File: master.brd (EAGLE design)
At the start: 56.1 x 93.9 mm, 77 parts, among them M1 DHT22-NP, M2 NRF24L01P-M, Q1 IRLML2502, U1 XMEGA-A3TQFP, U2 DS1302SOIC, U3 25LC640A-E/SN, U4 ENC28J60SO, U5 TS1117, X1 serial, X2 SPI/1W, X3 I2C, X4 ADC, X6 PS25_3W-R, X7 PS25_3W-R, X8 PS25_3W-R, X9 PS25_3W-R, Y1 25MHz

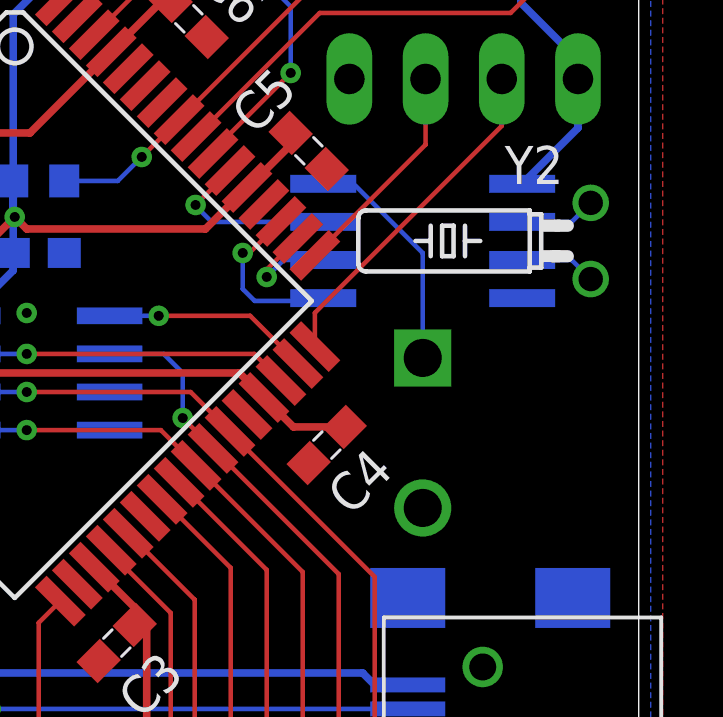
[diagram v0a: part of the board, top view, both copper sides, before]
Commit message: decoupling cap for rtc
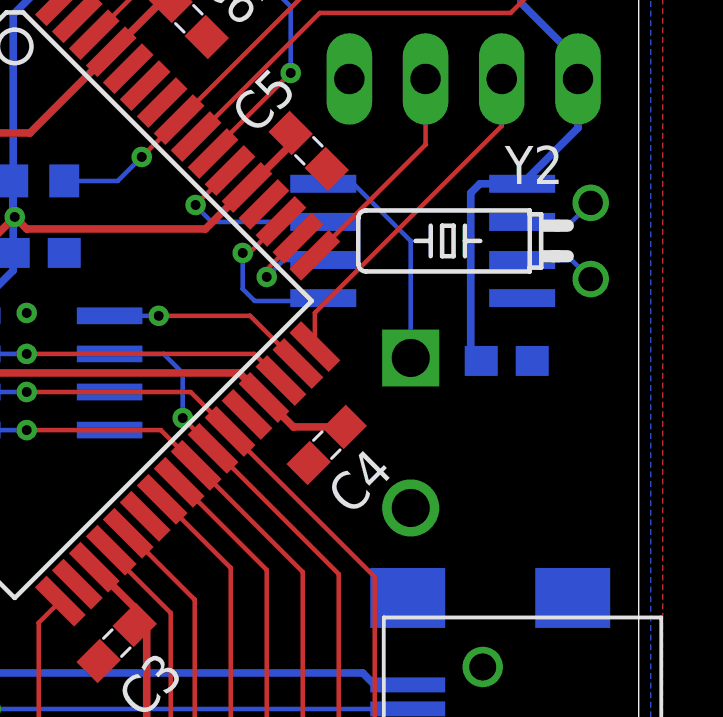
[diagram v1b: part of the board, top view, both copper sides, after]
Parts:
- added C24: 100n, rcl:C0603
- moved C14 0.40 mm to (48.4, 64.4)
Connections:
- net GND: now also C24.2
- net VCC: now also C24.1
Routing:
- net VCC: track 385.5 -> 393.1 mm

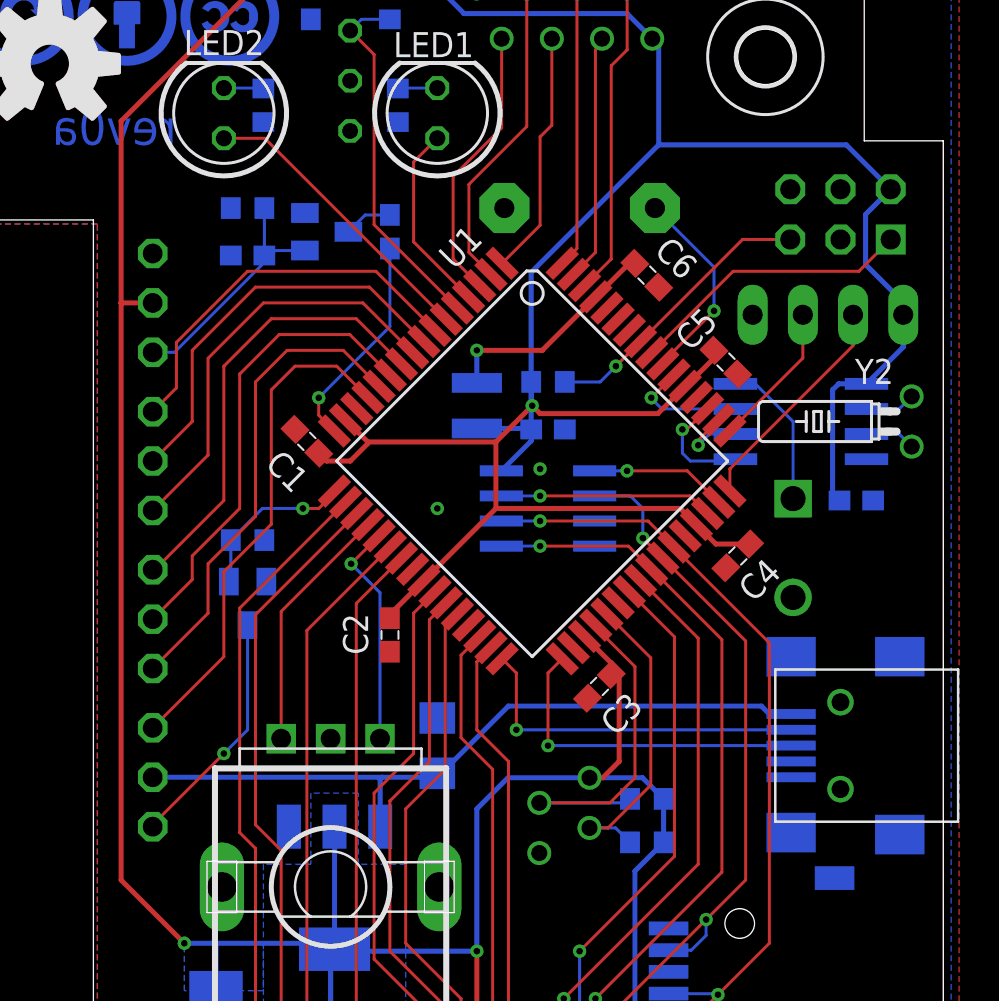
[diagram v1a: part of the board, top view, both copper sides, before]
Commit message: lcd connector changed to standard 2.54 pin header
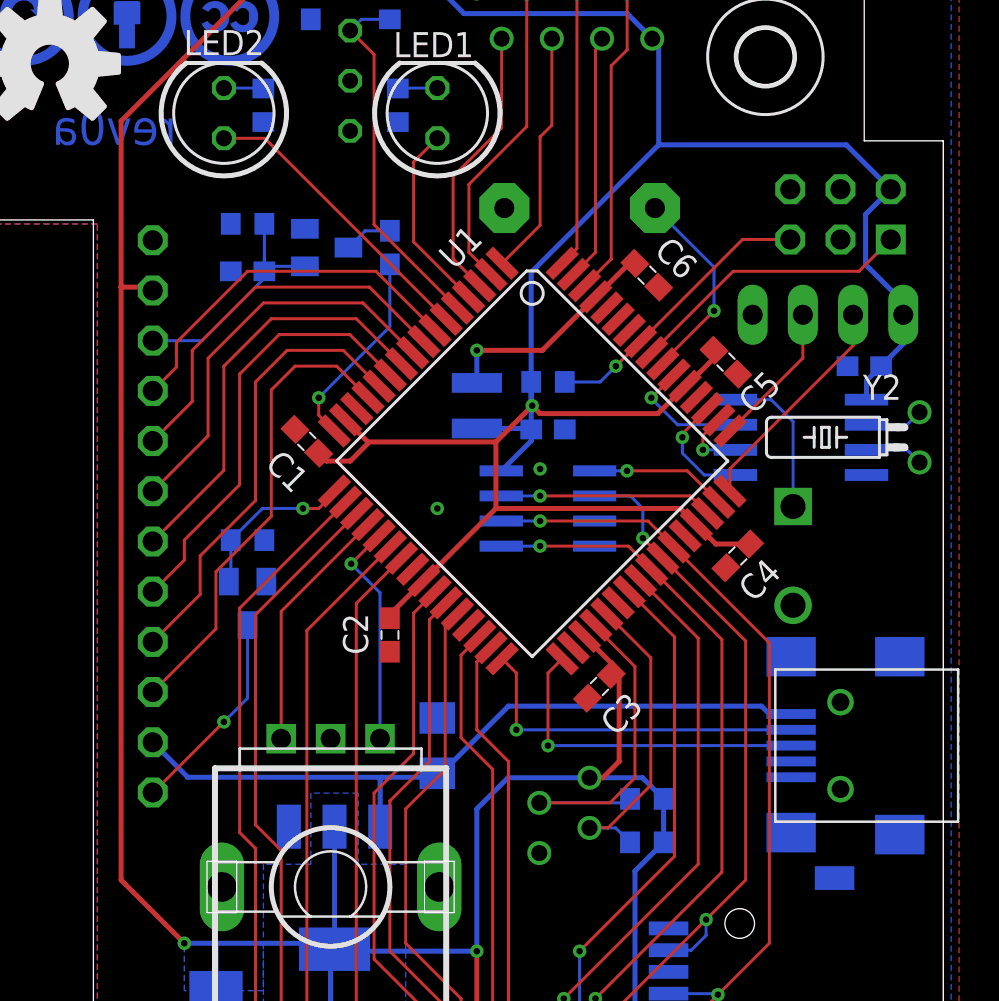
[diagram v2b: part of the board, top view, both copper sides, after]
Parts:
- removed X7, X8, X9: PS25_3W-R, con_PS25:PS25_3
- X6: value PS25_3W-R -> (none); device con_PS25:PS25_3 -> pinhead-mod:1X12R
- moved X6 10.8 mm to (16.0, 66.0)
- moved C24 6.81 mm to (52.0, 73.6), turned to 0 degrees
- moved Y2 0.89 mm to (54.8, 70.0)
- moved C11 0.80 mm to (28.0, 79.6)
- moved D1 0.80 mm to (24.8, 79.6)
- moved C10 0.80 mm to (20.8, 78.4)
- moved R3 0.80 mm to (20.8, 80.8)
- moved U2 0.80 mm to (48.8, 70.0)
- moved C14 0.40 mm to (48.4, 64.0)
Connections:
- net N$9 renamed LCD_V0
- removed net N$8: Q1.3, X9.3
- new net LCD_K: Q1.3, X6.12
- net +5V: now also X6.11; no longer X9.2
- net LCD_D4: now also X6.7; no longer X8.1
- net LCD_D5: now also X6.8; no longer X8.2
- net LCD_D6: now also X6.9; no longer X8.3
- net LCD_D7: now also X6.10; no longer X9.1
- net LCD_E: now also X6.6; no longer X7.3
- net LCD_RS: now also X6.4; no longer X7.1
- net LCR_RW: now also X6.5; no longer X7.2
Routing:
- net N$8: track 12.2 -> 0.00 mm, vias 1 -> 0
- net LCD_K: track 0.00 -> 10.5 mm, vias 0 -> 1
- net VCC: track 393.1 -> 386.4 mm
- net LCD_D7: track 25.6 -> 23.8 mm
- net LCD_D4: track 22.8 -> 21.3 mm
- net LCD_D5: track 23.5 -> 22.1 mm
- net LCD_D6: track 24.3 -> 23.0 mm
- net LCD_RS: track 19.8 -> 18.8 mm
- net LCR_RW: track 20.6 -> 19.6 mm
- net LCD_E: track 21.4 -> 20.4 mm
- net LCD_CONTR: track 11.2 -> 10.4 mm
- net +5V: track 36.8 -> 37.5 mm

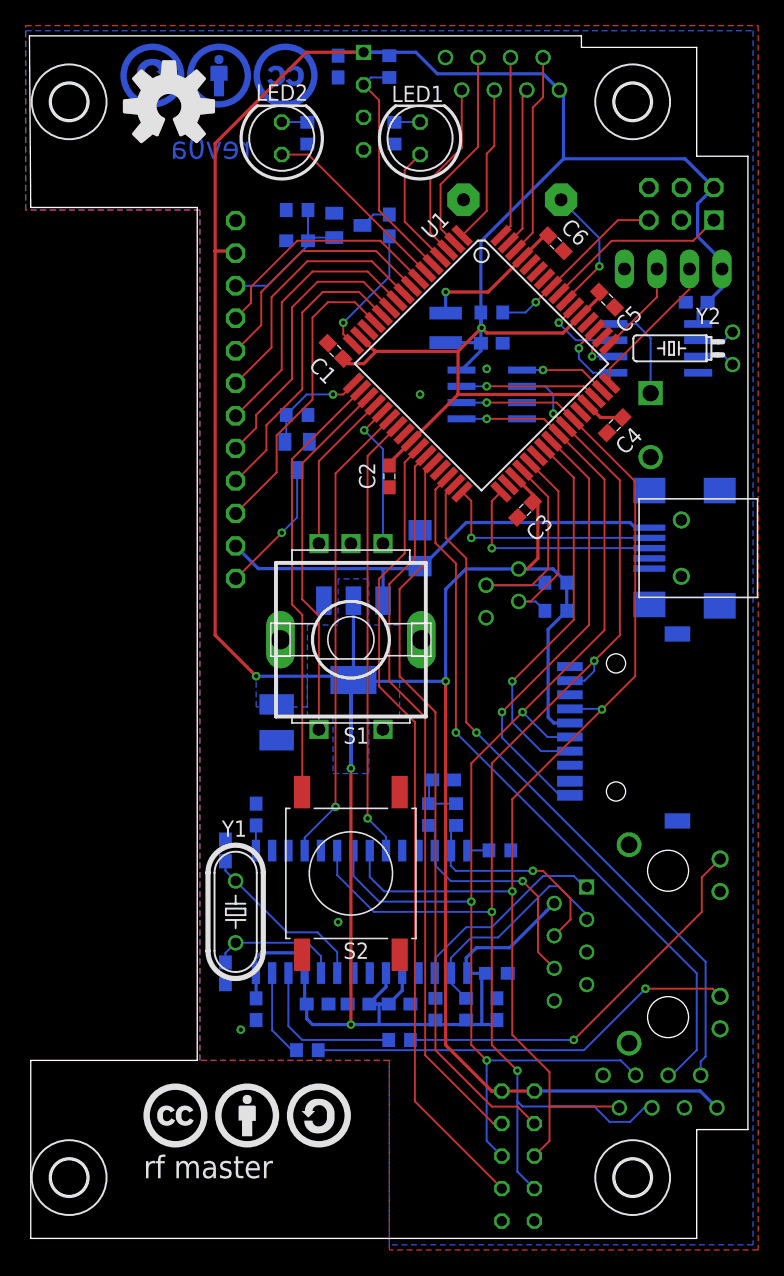
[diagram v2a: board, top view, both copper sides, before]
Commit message: dht22 sometimes hang, add mosfet as low side reset switch
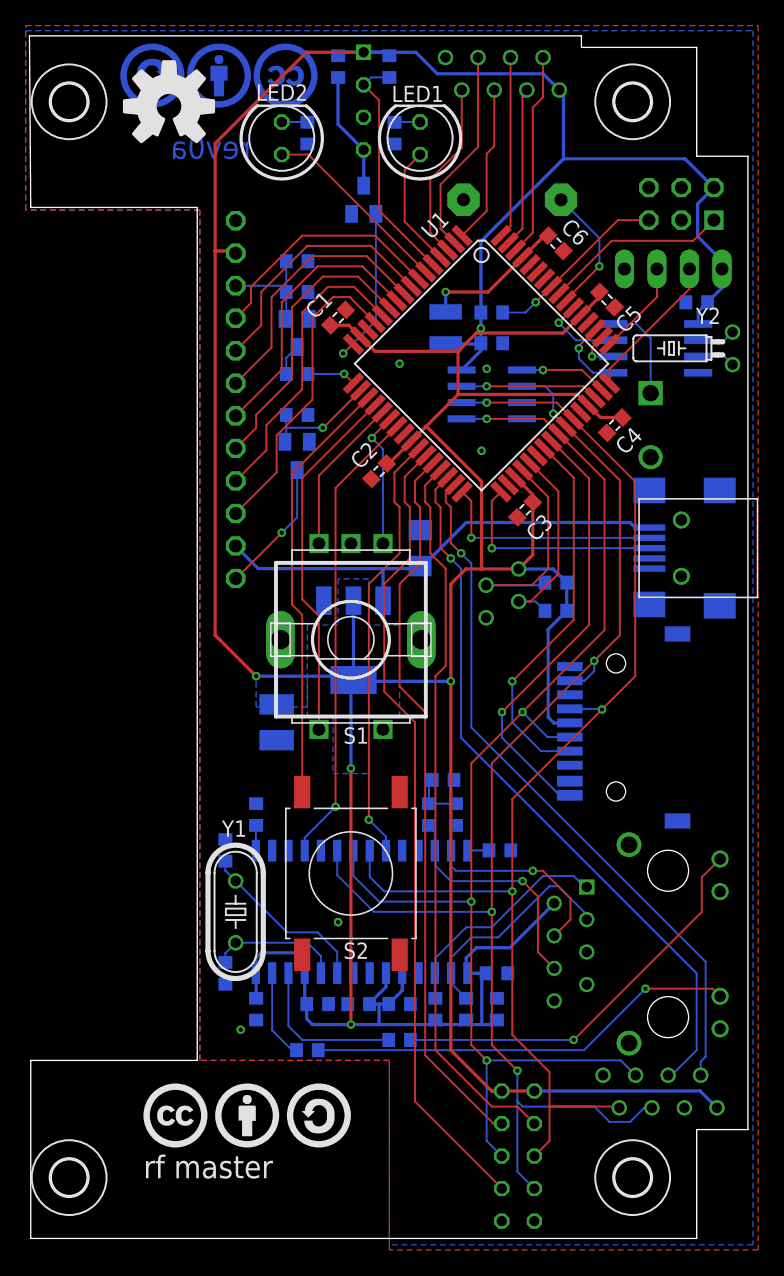
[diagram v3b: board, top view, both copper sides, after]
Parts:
- added Q2: IRLML2502, mosfet:MICRO3
- moved C11 13.7 mm to (20.8, 68.0), turned to 0 degrees
- moved D1 9.30 mm to (20.8, 71.2), turned to 180 degrees
- moved C10 4.00 mm to (20.8, 74.4), turned to 0 degrees
- moved R3 4.00 mm to (20.8, 76.8), turned to 0 degrees
- moved C1 2.61 mm to (24.0, 72.4), turned to 45 degrees
- moved C2 0.89 mm to (27.2, 60.4), turned to 225 degrees
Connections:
- new net DHTON: Q2.1, U1.16
- new net N$8: C9.1, M1.4, Q2.3
- net !LANCS: now also U1.26; no longer U1.23
- net !LANINT: now also U1.23; no longer U1.22
- net !RFCS: now also U1.28; no longer U1.27
- net GND: now also Q2.2; no longer C9.1, M1.4
- net LCD_BGLED: now also U1.18; no longer U1.17
- net LCD_CONTR: now also U1.17; no longer U1.16
- net RFCE: now also U1.29; no longer U1.28
- net RFIRQ: now also U1.27; no longer U1.26
- net S1A: now also U1.22; no longer U1.21
- net S1B: now also U1.21; no longer U1.20
- net S1P: now also U1.20; no longer U1.19
- net S2: now also U1.19; no longer U1.18
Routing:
- net DHTON: track 0.00 -> 13.0 mm, vias 0 -> 1
- net N$8: track 0.00 -> 9.28 mm
- net LCD_CONTR: track 10.4 -> 3.84 mm
- net VCC: track 386.4 -> 390.9 mm
- net LCD_V0: track 12.6 -> 9.04 mm
- net RFCE: track 58.2 -> 56.9 mm
- net S1A: track 11.5 -> 10.6 mm
- net !LANCS: track 34.7 -> 33.9 mm
- net LCD_BGLED: track 8.46 -> 9.16 mm
- net !RFCS: track 57.4 -> 56.7 mm
